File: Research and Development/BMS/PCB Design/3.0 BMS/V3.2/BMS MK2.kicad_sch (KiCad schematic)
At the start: 41 parts, among them J1 Conn_01x04_Socket, J5 CHG IN, Q1 AO3400A, Q2 PN100, Q3 AO3407, Q4 AO3407, SW1 SW_DPDT_x2, U1 ATTiny 85 Module, U3 TPS61040DBV, U4 MP1584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

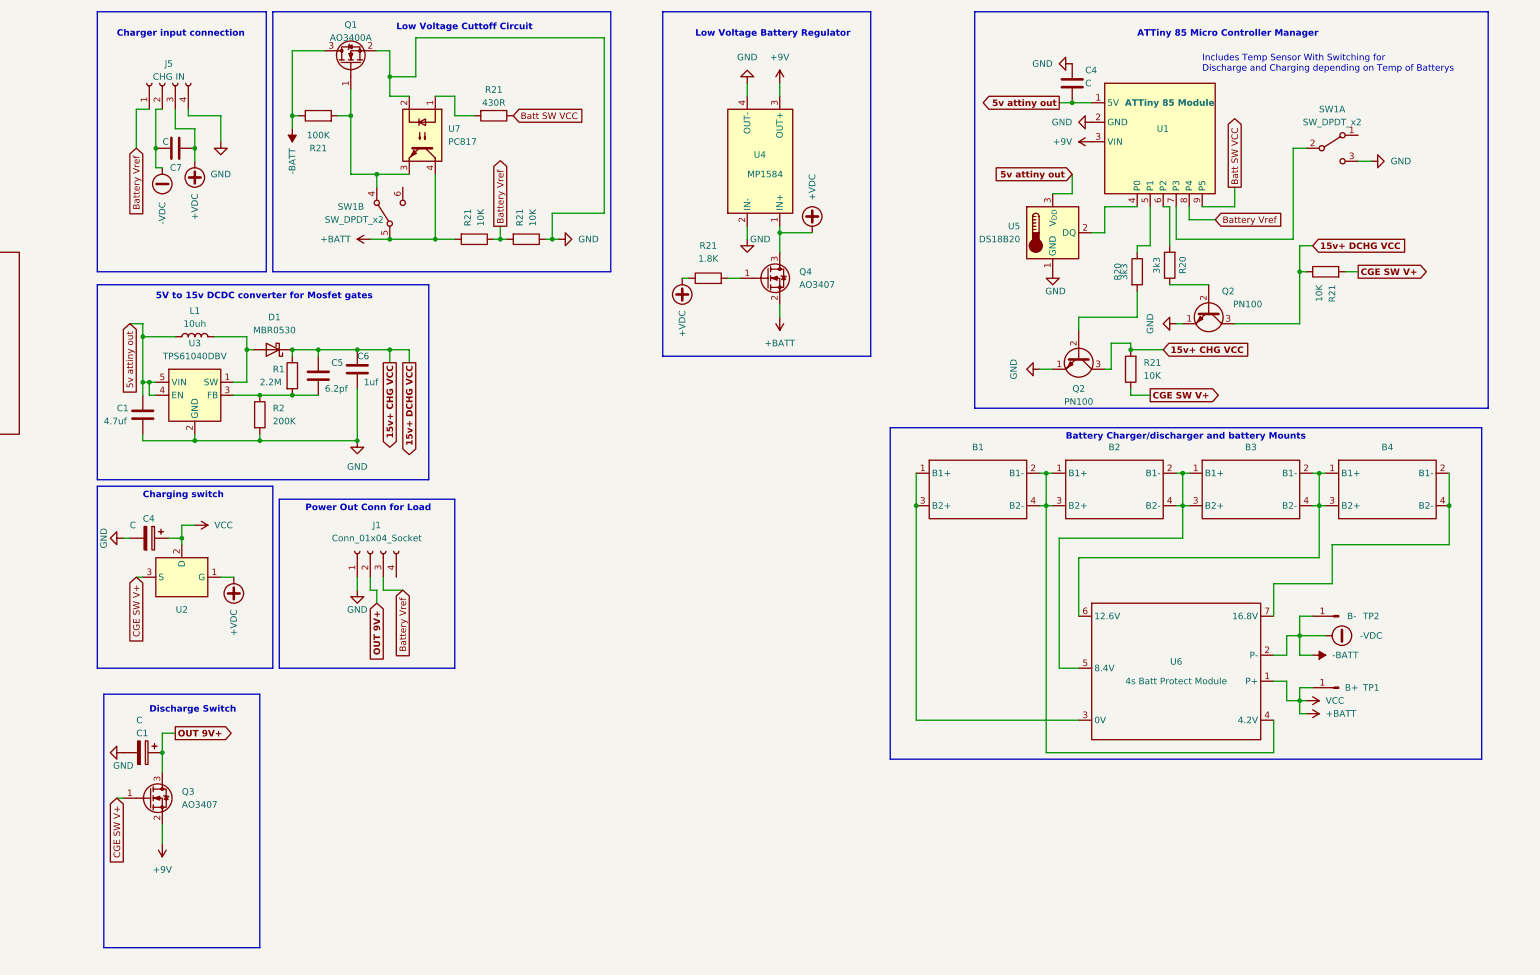
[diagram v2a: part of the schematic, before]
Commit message: updated bms schem
fixed polarity on batteries, updated jst conns to XH, created footprints for them, tidied up and shrunk the board size, changed from using the ds18d20b to a 10k ntc thermistor for temperature control protection
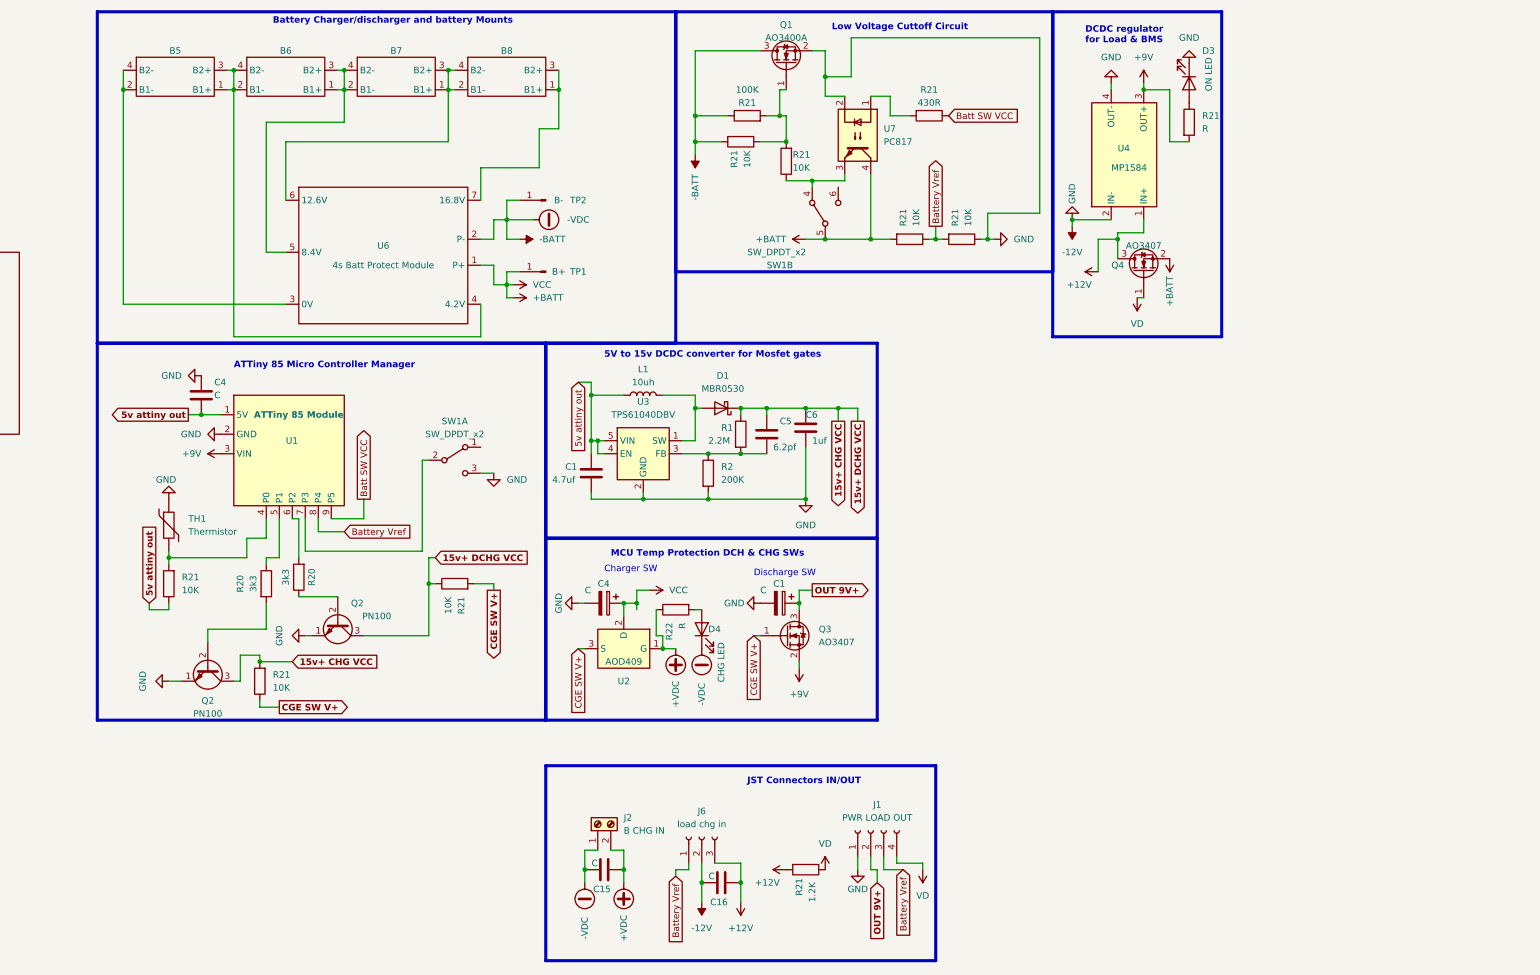
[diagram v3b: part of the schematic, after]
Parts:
- removed B1, B2, B3, B4: ~, DCDC buck converter lm2596:18650 Batt 2S Holder, symbol BMS-MK2-symbols:18650_Bat_pair
- removed C7: C, symbol Device:C
- removed J5: CHG IN, Connector_JST:JST_GH_SM04B-GHS-TB_1x04-1MP_P1.25mm_Horizontal, symbol Connector:Conn_01x04_Socket
- removed R21: 1.8K, Resistor_SMD:R_1206_3216Metric, symbol Device:R
- removed U5: DS18B20, Package_TO_SOT_THT:TO-92_Inline, symbol Sensor_Temperature:DS18B20
- added B5, B6, B7, B8: ~, DCDC buck converter lm2596:18650 Batt 2S Holder, symbol New_Library:battery_2p_holder
- added C15, C16: C, symbol Device:C
- added D3: ON LED, LED_SMD:LED_1206_3216Metric, symbol Device:LED
- added D4: CHG LED, LED_SMD:LED_1206_3216Metric, symbol Device:LED
- added J2: B CHG IN, DCDC buck converter lm2596:kf1000 screw terminal, symbol Connector:Screw_Terminal_01x02
- added J6: load chg in, DCDC buck converter lm2596:XH 2.54mm 3p smd vertical header, symbol Connector:Conn_01x03_Socket
- added R21 (x3): 10K, Resistor_SMD:R_1206_3216Metric, symbol Device:R
- added R21, R22: R, Resistor_SMD:R_1206_3216Metric, symbol Device:R
- added R21: 1.2K, Resistor_SMD:R_1206_3216Metric, symbol Device:R
- added TH1: Thermistor, Resistor_THT:R_Axial_DIN0204_L3.6mm_D1.6mm_P7.62mm_Horizontal, symbol Device:Thermistor
- J1: value Conn_01x04_Socket -> PWR LOAD OUT; footprint Connector_JST:JST_GH_SM04B-GHS-TB_1x04-1MP_P1.25mm_Horizontal -> DCDC buck converter lm2596:XH 2.54mm 4p vertical header
- Q1: Specs (none) -> 30V, 5.7A, +-12V VGS
- Q3, Q4: Specs (none) -> 30V 4.1A +-20V VGS
- SW1: switch type (none) -> SH T80R
- U2: value ~ -> AOD409; Specs (none) -> 60V 26A
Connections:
- net +9V: now also R21.2
- net +VDC: now also C15.2, J2.2 (Pin_2), R22.1; no longer Q4.3 (D), U4.1 (IN+)
- net -BATT: now also C15.1, D4.1 (K), J2.1 (Pin_1), R21.2
- net 5v attiny out: now also R21.1
- net Battery Vref: now also J6.1 (Pin_1)
- net at U1.4 (P0): now also R21.2, TH1.2
- net VD: now reaches Q4.1 (G)
- net VD: now also J1.4 (Pin_4), R21.1
- net at Q1.1 (G), R21.2: now also R21.1, R21.2; no longer SW1.4 (A), U7.3
- net at U6.6 (12.6V): now also B7.1 (B1+), B7.3 (B2+), B8.2 (B1-), B8.4 (B2-)
- net at U6.7 (16.8V): now also B8.1 (B1+), B8.3 (B2+)
- net at U6.5 (8.4V): now also B6.1 (B1+), B6.3 (B2+), B7.2 (B1-), B7.4 (B2-)
- net at U6.4 (4.2V): now also B5.1 (B1+), B5.3 (B2+), B6.2 (B1-), B6.4 (B2-)
- net at U6.3 (0V): now also B5.2 (B1-), B5.4 (B2-)
- net GND renamed -12V
- net -12V: now also C16.1, D3.1 (K), J6.2 (Pin_2), TH1.1
- new net: D3.2 (A), R21.1
- new net: R21.1, SW1.4 (A), U7.3
- new net: D4.2 (A), R22.2
- new net +12V: C16.2, J6.3 (Pin_3), Q4.3 (D), R21.2, U4.1 (IN+)
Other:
- note added: "Charger SW"
- note added: "DCDC regulator for Load & BMS"
- note added: "Discharge SW"
- note added: "JST Connectors IN/OUT"
- note added: "MCU Temp Protection DCH & CHG SWs"
- note removed: "Charger input connection"
- note removed: "Charging switch"
- note removed: "Discharge Switch"
- note removed: "Includes Temp Sensor With Switching for Discharge and Charging depending on Temp of Batterys"
- note removed: "Low Voltage Battery Regulator"
- note removed: "Power Out Conn for Load"
- moved on the sheet: C1, C4, C5, C6, D1, J1, L1, Q1, Q2, Q3, Q4, R1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

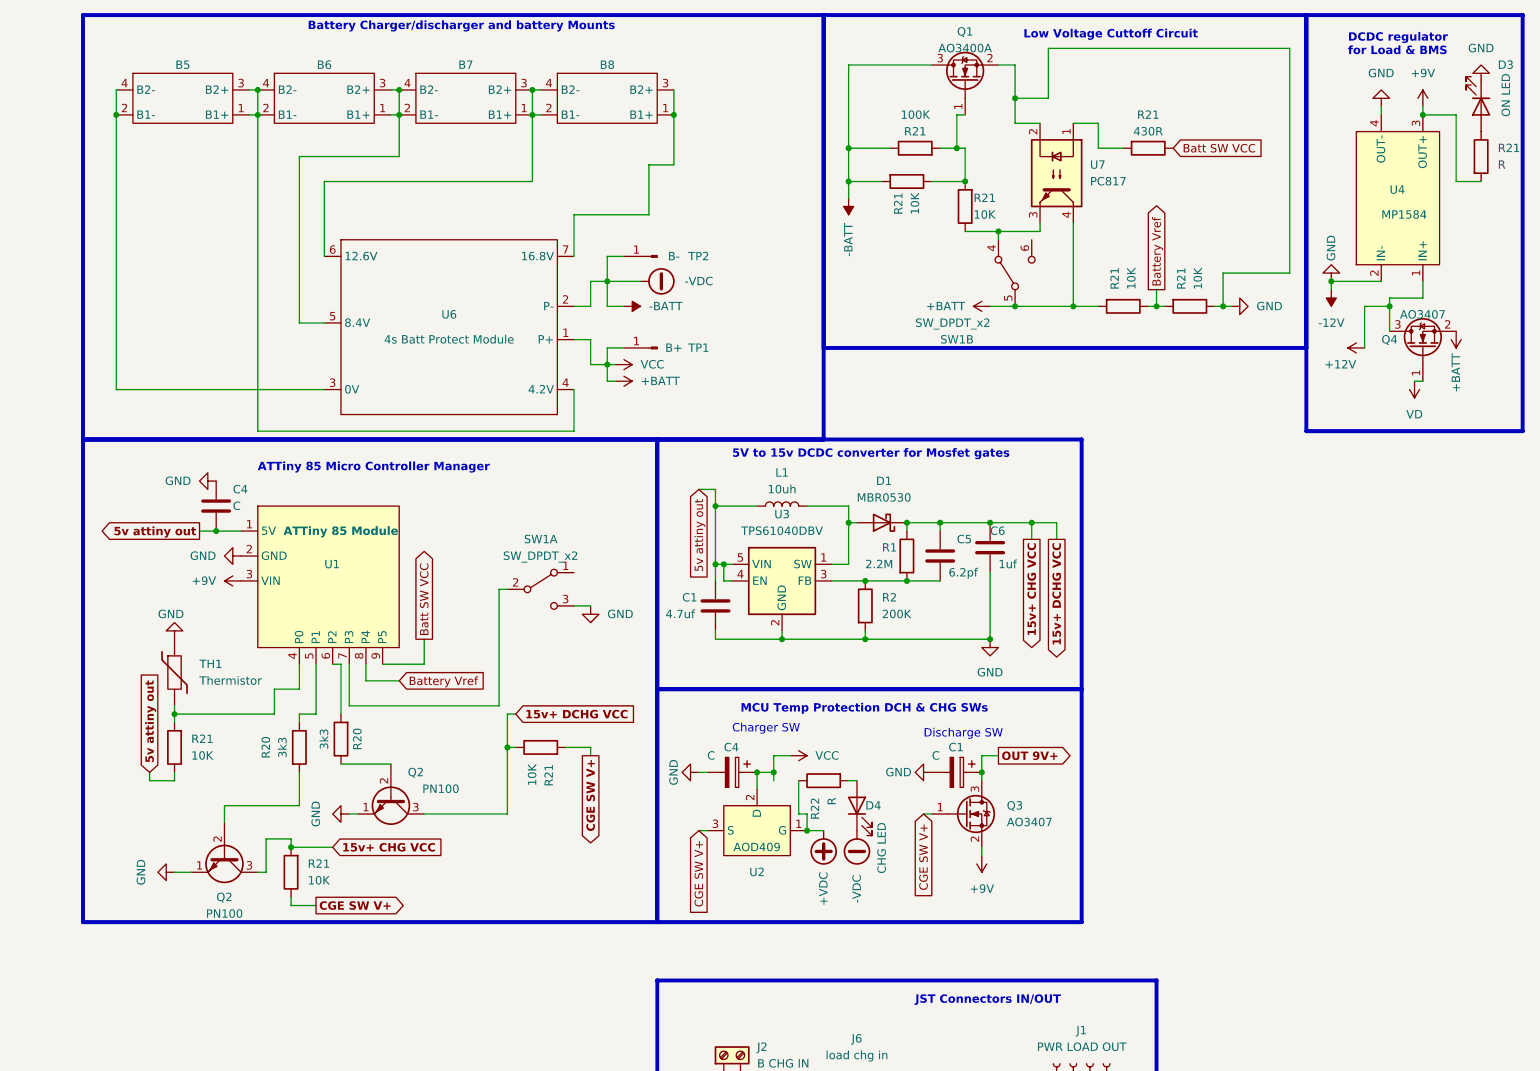
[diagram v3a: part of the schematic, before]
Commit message: redone bms board and added test bms schem and board to test functionality without the batteries
added:
- bms test schem and layout
- updated bms
- testing of quad rotary encoder breakout board
- testing of teensy audio board
- combining the encoders and audio board in 1 circuit with limited control of chorus fx with encoders
- created text based skeleton structure of GUI of the interface with use of encoders and home button
- created file for adding fx functionality. will be now incorperating fx
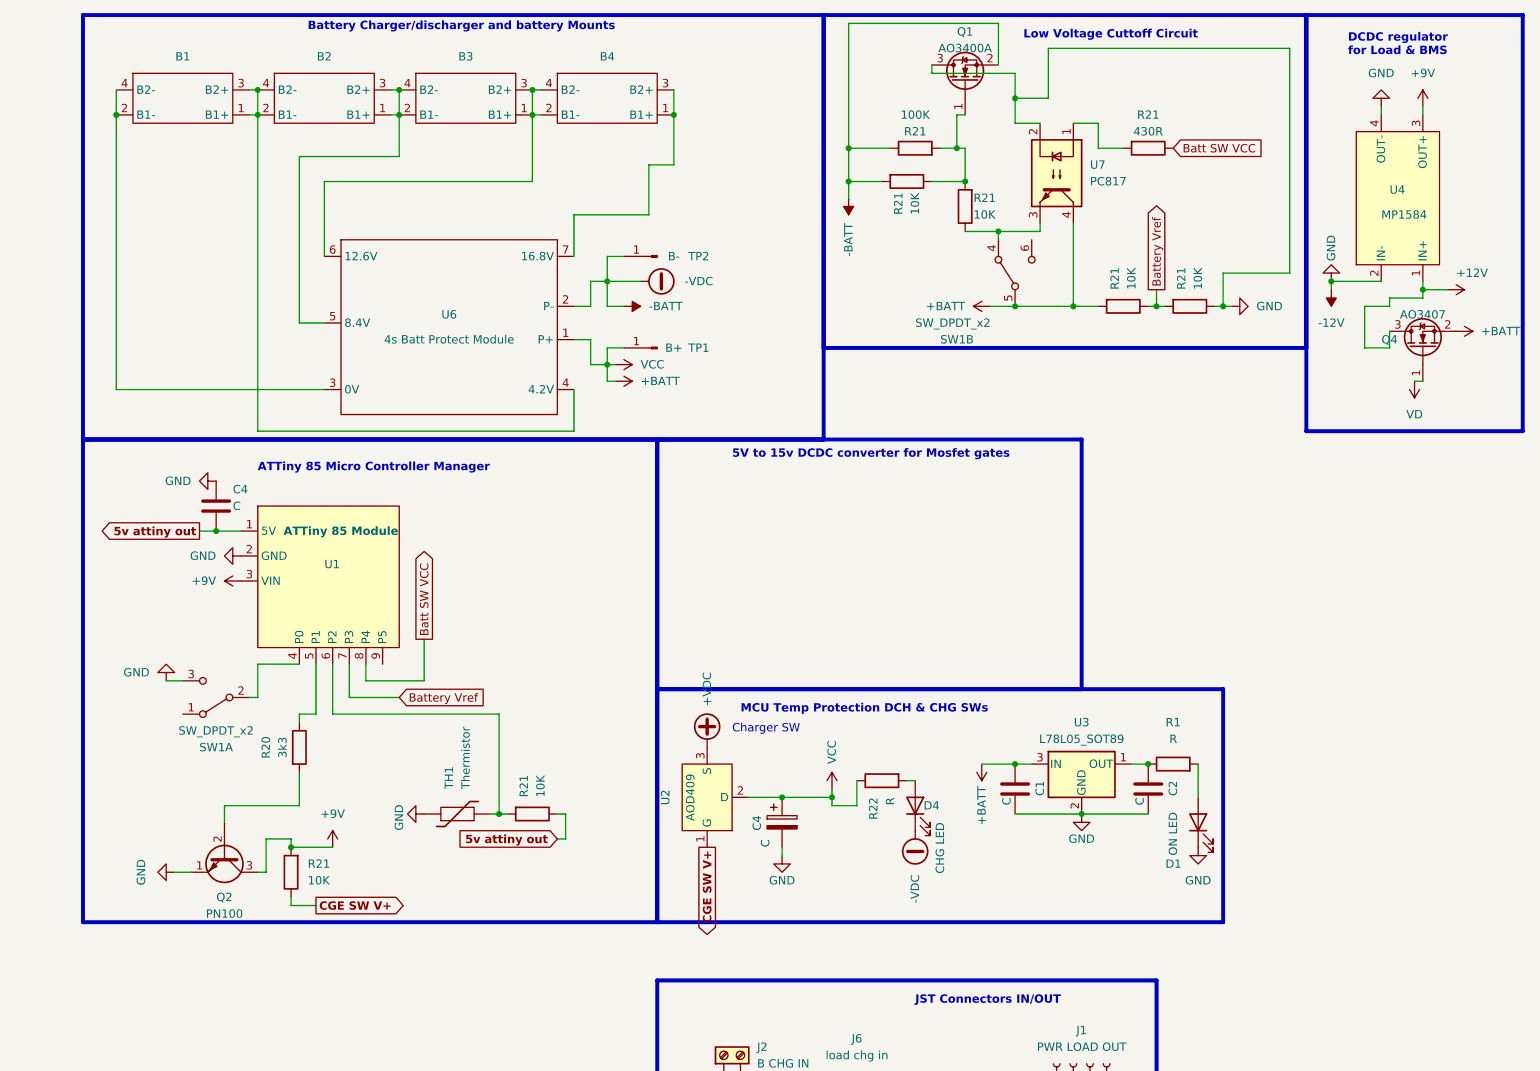
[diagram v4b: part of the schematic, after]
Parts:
- removed C1: C, symbol Device:C_Polarized
- removed C5: 6.2pf, Capacitor_SMD:C_1206_3216Metric, symbol Device:C
- removed C6: 1uf, Capacitor_SMD:C_1206_3216Metric, symbol Device:C
- removed D1: MBR0530, Diode_SMD:D_SOD-123, symbol Diode:MBR0530
- removed D3: ON LED, LED_SMD:LED_1206_3216Metric, symbol Device:LED
- removed L1: 10uh, Inductor_SMD:L_6.3x6.3_H3, symbol Device:L
- removed Q2: PN100, Package_TO_SOT_SMD:SOT-23, symbol Transistor_BJT:PN2222A
- removed Q3: AO3407, Package_TO_SOT_SMD:SOT-23, symbol Transistor_FET:AO3400A
- removed R2: 200K, Resistor_SMD:R_1206_3216Metric, symbol Device:R
- removed R20: 3k3, Resistor_SMD:R_1206_3216Metric, symbol Device:R
- removed R21: R, Resistor_SMD:R_1206_3216Metric, symbol Device:R
- removed R21: 10K, Resistor_SMD:R_1206_3216Metric, symbol Device:R
- removed U3: TPS61040DBV, Package_TO_SOT_SMD:SOT-23-5, symbol Regulator_Switching:TPS61040DBV
- added C2: C, Capacitor_SMD:C_1206_3216Metric, symbol Device:C
- added D1: ON LED, LED_SMD:LED_1206_3216Metric, symbol Device:LED
- added U3: L78L05_SOT89, Package_TO_SOT_SMD:SOT-89-3, symbol Regulator_Linear:L78L05_SOT89
- C1: value 4.7uf -> C
- R1: value 2.2M -> R
- renumbered B5 to B1, B6 to B2, B7 to B3, B8 to B4
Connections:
- net +9V: now also Q2.3 (C), R21.2
- net +BATT: now also C1.2, R22.1, U3.3 (IN)
- net +VDC: now also U2.3 (S); no longer R22.1, U2.1 (G)
- net -12V: now also Q1.3 (D), C2.1, D1.1 (K), U3.2 (GND); no longer Q1.2 (S)
- net -BATT: now also Q1.2 (S); no longer Q1.3 (D)
- net 5v attiny out: no longer C1.2
- net Batt SW VCC: now also U1.8 (P4); no longer U1.9 (P5)
- net Battery Vref: now also U1.7 (P3); no longer U1.8 (P4)
- net CGE SW V+: now also U2.1 (G); no longer U2.3 (S)
- net at SW1.2 (B): now also U1.4 (P0); no longer U1.7 (P3)
- net at R1.2: now also D1.2 (A)
- net at U1.6 (P2): now also R21.2, TH1.2
- removed net 15v+ CHG VCC: Q2.3 (C), R1.1, R21.2
- new net: C2.2, R1.1, U3.1 (OUT)
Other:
- note removed: "Discharge SW"
- moved on the sheet: C4, D4, R21, R22, SW1A, TH1
